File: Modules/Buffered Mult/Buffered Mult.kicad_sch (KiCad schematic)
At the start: 21 parts, among them J1 0V

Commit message: Updated fps to 12mm diameter
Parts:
- H1, H2, H3, H4: footprint SynthStuff:MountingHole_3.2mm_M3_Pad4mm -> SynthStuff:MountingHole_Rails
- H10, H11, H12, H15, H16, H17, H18, H19, H20, H7, H8, H9: footprint SynthStuff:Jack_6.35mm_Cutout_Output_v5 -> SynthStuff:Jack_6.35mm_Cutout_Output_v6
- H13, H14, H5, H6: footprint SynthStuff:Jack_6.35mm_Cutout_v2 -> SynthStuff:Jack_6.35mm_Cutout_v3
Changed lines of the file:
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@@
 			)
 		)
-		(property "Footprint" "SynthStuff:Jack_6.35mm_Cutout_v2"
+		(property "Footprint" "SynthStuff:Jack_6.35mm_Cutout_v3"
 			(at 190.5 88.9 0)
 			(effects
@@
 			)
 		)
-		(property "Footprint" "SynthStuff:Jack_6.35mm_Cutout_Output_v5"
+		(property "Footprint" "SynthStuff:Jack_6.35mm_Cutout_Output_v6"
 			(at 152.4 38.1 0)
 			(effects
@@
 			)
 		)
-		(property "Footprint" "SynthStuff:MountingHole_3.2mm_M3_Pad4mm"
+		(property "Footprint" "SynthStuff:MountingHole_Rails"
 			(at 88.9 64.77 0)
 			(effects
@@
 			)
 		)
-		(property "Footprint" "SynthStuff:Jack_6.35mm_Cutout_Output_v5"
+		(property "Footprint" "SynthStuff:Jack_6.35mm_Cutout_Output_v6"
 			(at 152.4 50.8 0)
 			(effects
@@
 			)
 		)
-		(property "Footprint" "SynthStuff:Jack_6.35mm_Cutout_Output_v5"
+		(property "Footprint" "SynthStuff:Jack_6.35mm_Cutout_Output_v6"
 			(at 190.5 114.3 0)
 			(effects
@@
 			)
 		)
-		(property "Footprint" "SynthStuff:Jack_6.35mm_Cutout_v2"
+		(property "Footprint" "SynthStuff:Jack_6.35mm_Cutout_v3"
 			(at 152.4 88.9 0)
 			(effects
@@
 			)
 		)
-		(property "Footprint" "SynthStuff:MountingHole_3.2mm_M3_Pad4mm"
+		(property "Footprint" "SynthStuff:MountingHole_Rails"
 			(at 63.5 77.47 0)
 			(effects
@@
 			)
 		)
-		(property "Footprint" "SynthStuff:MountingHole_3.2mm_M3_Pad4mm"
+		(property "Footprint" "SynthStuff:MountingHole_Rails"
 			(at 63.5 64.77 0)
 			(effects
@@
 			)
 		)
-		(property "Footprint" "SynthStuff:Jack_6.35mm_Cutout_v2"
+		(property "Footprint" "SynthStuff:Jack_6.35mm_Cutout_v3"
 			(at 190.5 25.4 0)
 			(effects
@@
 			)
 		)
-		(property "Footprint" "SynthStuff:Jack_6.35mm_Cutout_Output_v5"
+		(property "Footprint" "SynthStuff:Jack_6.35mm_Cutout_Output_v6"
 			(at 152.4 101.6 0)
 			(effects
@@
 			)
 		)
-		(property "Footprint" "SynthStuff:Jack_6.35mm_Cutout_Output_v5"
+		(property "Footprint" "SynthStuff:Jack_6.35mm_Cutout_Output_v6"
 			(at 190.5 127 0)
 			(effects
@@
 			)
 		)
-		(property "Footprint" "SynthStuff:Jack_6.35mm_Cutout_Output_v5"
+		(property "Footprint" "SynthStuff:Jack_6.35mm_Cutout_Output_v6"
 			(at 190.5 63.5 0)
 			(effects
@@
 			)
 		)
-		(property "Footprint" "SynthStuff:Jack_6.35mm_Cutout_Output_v5"
+		(property "Footprint" "SynthStuff:Jack_6.35mm_Cutout_Output_v6"
 			(at 152.4 63.5 0)
 			(effects
@@
 			)
 		)
-		(property "Footprint" "SynthStuff:Jack_6.35mm_Cutout_Output_v5"
+		(property "Footprint" "SynthStuff:Jack_6.35mm_Cutout_Output_v6"
 			(at 190.5 50.8 0)
 			(effects
@@
 			)
 		)
-		(property "Footprint" "SynthStuff:Jack_6.35mm_Cutout_Output_v5"
+		(property "Footprint" "SynthStuff:Jack_6.35mm_Cutout_Output_v6"
 			(at 152.4 114.3 0)
 			(effects
@@
 			)
 		)
-		(property "Footprint" "SynthStuff:Jack_6.35mm_Cutout_Output_v5"
+		(property "Footprint" "SynthStuff:Jack_6.35mm_Cutout_Output_v6"
 			(at 190.5 38.1 0)
 			(effects
@@
 			)
 		)
-		(property "Footprint" "SynthStuff:MountingHole_3.2mm_M3_Pad4mm"
+		(property "Footprint" "SynthStuff:MountingHole_Rails"
 			(at 88.9 77.47 0)
 			(effects
@@
 			)
 		)
-		(property "Footprint" "SynthStuff:Jack_6.35mm_Cutout_Output_v5"
+		(property "Footprint" "SynthStuff:Jack_6.35mm_Cutout_Output_v6"
 			(at 152.4 127 0)
 			(effects
@@
 			)
 		)
-		(property "Footprint" "SynthStuff:Jack_6.35mm_Cutout_Output_v5"
+		(property "Footprint" "SynthStuff:Jack_6.35mm_Cutout_Output_v6"
 			(at 190.5 101.6 0)
 			(effects
@@
 			)
 		)
-		(property "Footprint" "SynthStuff:Jack_6.35mm_Cutout_v2"
+		(property "Footprint" "SynthStuff:Jack_6.35mm_Cutout_v3"
 			(at 152.4 25.4 0)
 			(effects

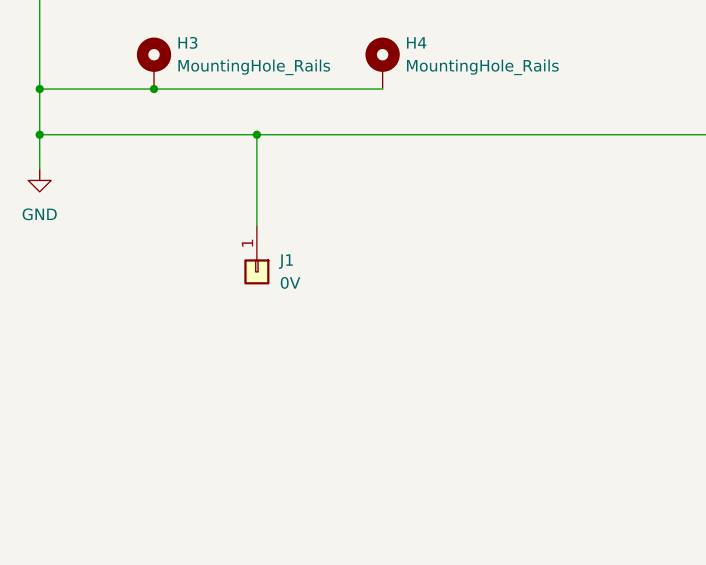
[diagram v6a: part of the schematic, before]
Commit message: Updated jack footprints to 12mm washer
... and added hash art to Adapter Mult CV and Gate jacks
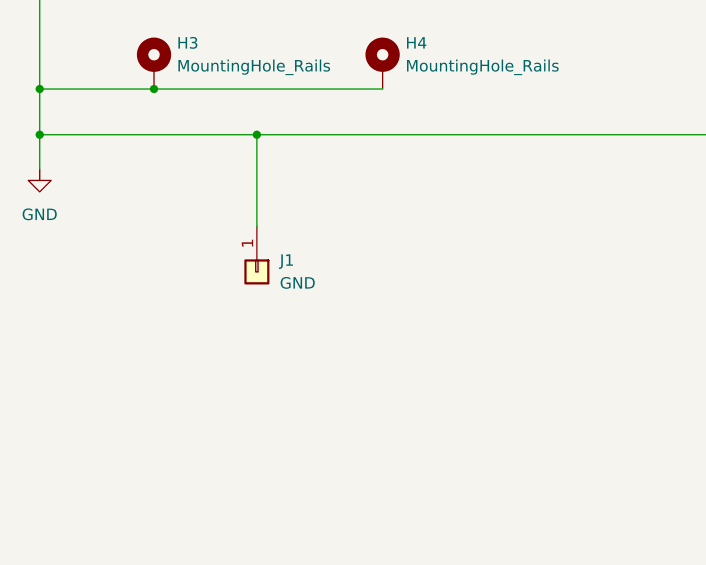
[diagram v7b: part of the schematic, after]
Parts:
- J1: value 0V -> GND
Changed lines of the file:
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@@
 			)
 		)
-		(property "Value" "0V"
+		(property "Value" "GND"
 			(at 77.47 101.5999 90)
 			(effects
